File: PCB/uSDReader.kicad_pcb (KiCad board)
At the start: 2 copper layers, 53.6 x 25 mm, 34 parts, among them IC1 USB2244I-AEZG-06-TR, J1 Micro_SD_Card_Det1, J2 USB_A, U1 LM1117MP-3.3, Y2 Crystal 24MHz (±350 ppm)

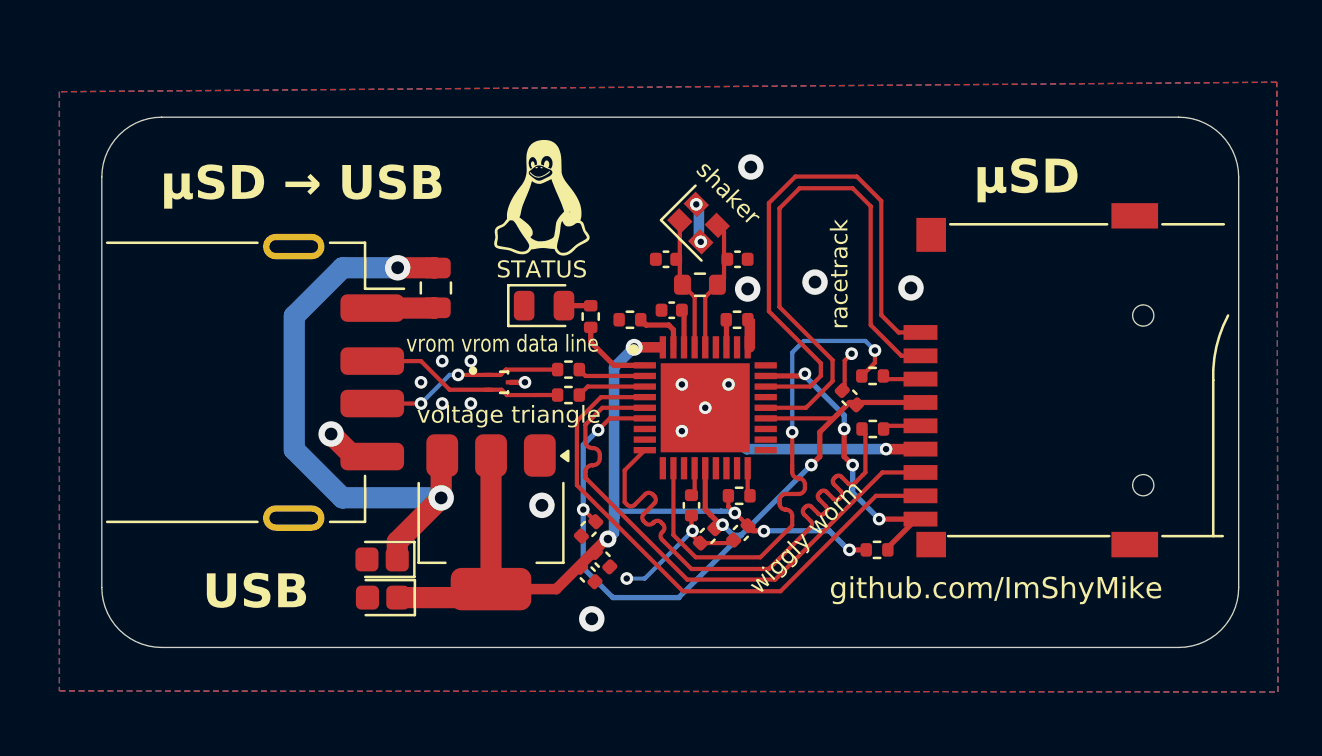
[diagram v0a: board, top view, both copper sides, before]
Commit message: REV 4
Swapped the voltage regulator and the status LED and cleaned up traces
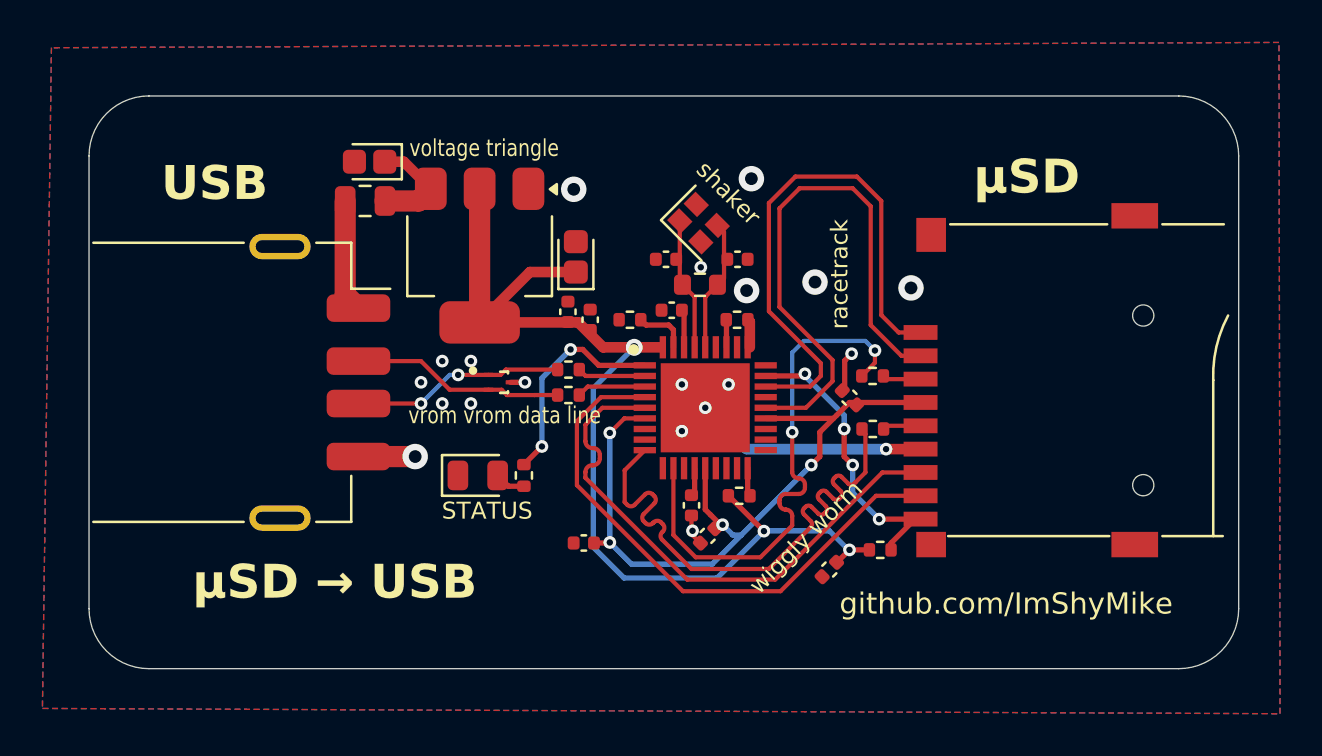
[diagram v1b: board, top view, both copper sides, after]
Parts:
- removed the G*** at (95.2, 60.2)
- C11, C12: value 2pf -> Ceramic 12 pF ± 5%
- moved C1 18.8 mm to (87.1, 58.5)
- moved C2 18.5 mm to (96.8, 63.0), turned to 90 degrees
- moved U1 12.6 mm to (92.3, 62.9)
- moved C9 12.4 mm to (96.4, 65.6), turned to -90 degrees
- moved C8 11.3 mm to (97.5, 66.0), turned to 90 degrees
- moved D2 8.59 mm to (92.2, 73.3)
- moved R7 8.13 mm to (94.3, 73.3), turned to 90 degrees
- moved F1 5.29 mm to (86.9, 60.4), turned to 0 degrees
- moved C10 4.52 mm to (108.8, 77.7)
- moved C4 0.70 mm to (97.2, 76.5), turned to 180 degrees
- moved J2 0.65 mm to (79.3, 68.9)
- moved R10 0.15 mm to (111.2, 76.8)
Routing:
- net +5V: track 27.4 -> 5.10 mm, vias 2 -> 0
- net +3.3V: track 41.4 -> 52.0 mm, vias 5 -> 3
- net GND: track 15.4 -> 8.15 mm, vias 18 -> 15
- net Net-(IC1-LED): track 3.70 -> 10.1 mm, vias 0 -> 2
- net VDD3: track 39.2 -> 34.9 mm
- net Net-(J2-VBUS): track 2.96 -> 5.31 mm
- net D-: track 9.40 -> 10.1 mm
- net D+: track 9.40 -> 10.1 mm
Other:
- board size 53.6 x 25 mm -> 54.2 x 27 mm
- board text added: "REV 4"
- board text removed: "REV 3"
